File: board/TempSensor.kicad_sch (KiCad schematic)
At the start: 1 part, among them U6 MCP9808-E/MS

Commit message: Added most Footprints, Schematic review touch up
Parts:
- U6: footprint MSOP8_MC_MCH -> (none)
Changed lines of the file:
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@@
 			)
 		)
-		(property "Footprint" "MSOP8_MC_MCH"
+		(property "Footprint" ""
 			(at 118.11 92.71 0)
 			(effects

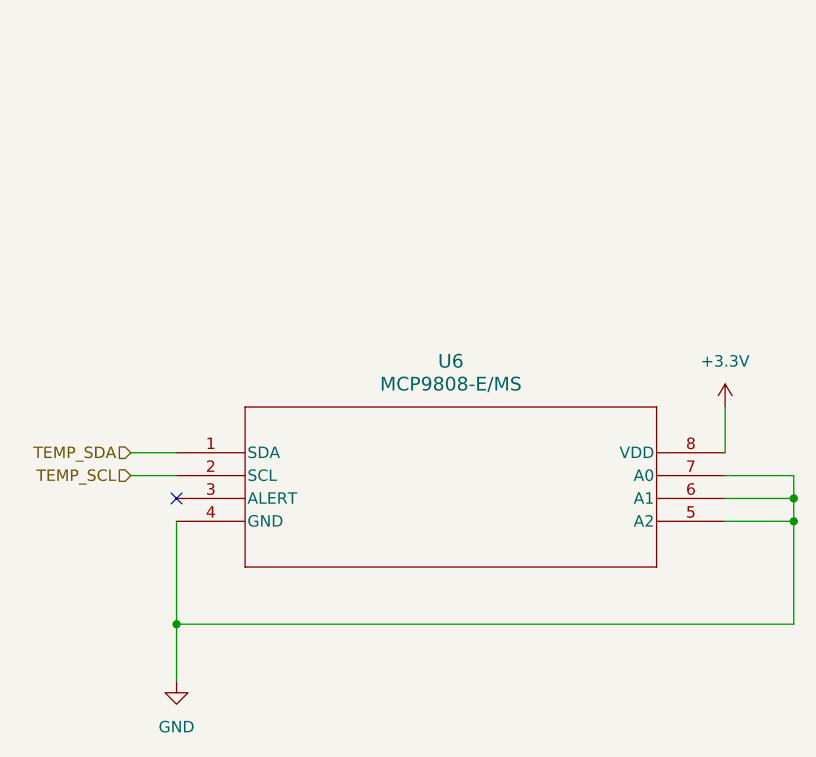
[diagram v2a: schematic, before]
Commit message: Cleaned up traces and silkscreens
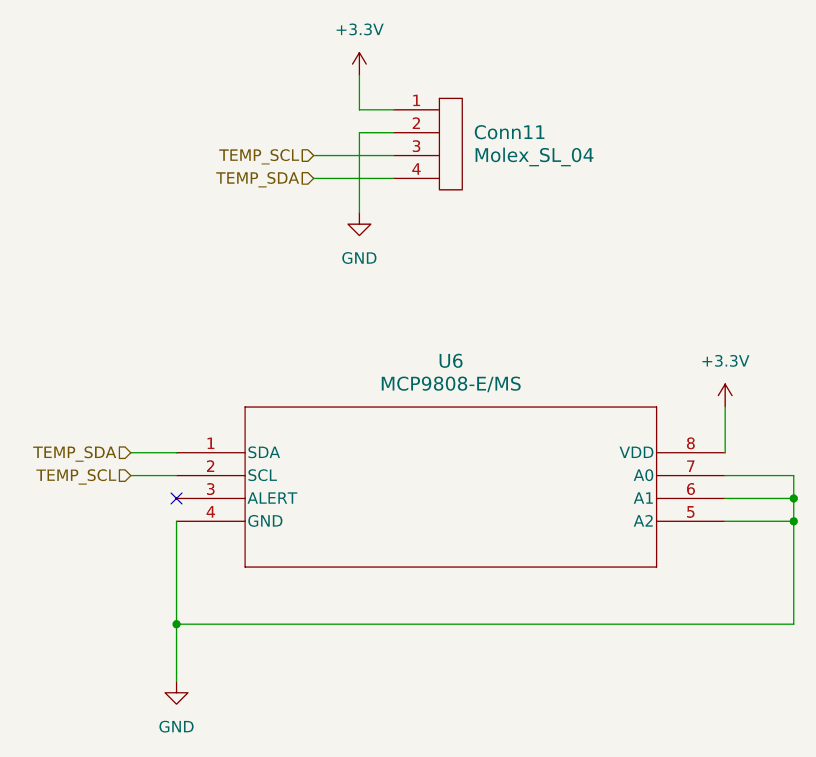
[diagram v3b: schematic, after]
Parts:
- added Conn11: Molex_SL_04, MRDT_Connectors:MOLEX_SL_04_Vertical, symbol MRDT_Connectors:Molex_SL_04
- U6: footprint (none) -> CoreBoard:MSOP8_MC_MCH-L
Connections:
- net +3.3V: now also Conn11.1
- net GND: now also Conn11.2
- net TEMP_SCL: now also Conn11.3
- net TEMP_SDA: now also Conn11.4
